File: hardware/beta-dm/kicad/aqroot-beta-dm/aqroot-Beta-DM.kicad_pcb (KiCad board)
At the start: 4 copper layers, 74 x 155 mm, 188 parts, among them J1 CH280QV10-CT_50P, J2 Molex_5025700893, J3 USB_C_Receptacle_USB2.0_16P, J4 JST-PH-2 BATTERY, J5 COMMUNITY_HEADER_2x13, J6 JST-PH-2 SPEAKER, Q1 AO3400A, SW1 BOOT, SW2 UP, SW3 DOWN, SW4 LEFT, SW5 RIGHT, SW6 A_SELECT, SW7 B_BACK, SW8 HOME, SW9 SW_SPDT, U1 ESP32-S3-WROOM-1, U10 USBLC6-2SC6, U11 BQ25185, U12 TPS63020, U13 TPS61023, U14 MAX17048, U15 TPS22918, U16 TCA9517ADGK, U17 TPS61169DCKR, U2 TCA9535PWR, U3 TCA9535PWR, U4 BMI270, U5 MAX98357A, U6 TSOP38238, U7 E07-400M10S, U8 E22-900M22S, U9 ST25R3916-AQET

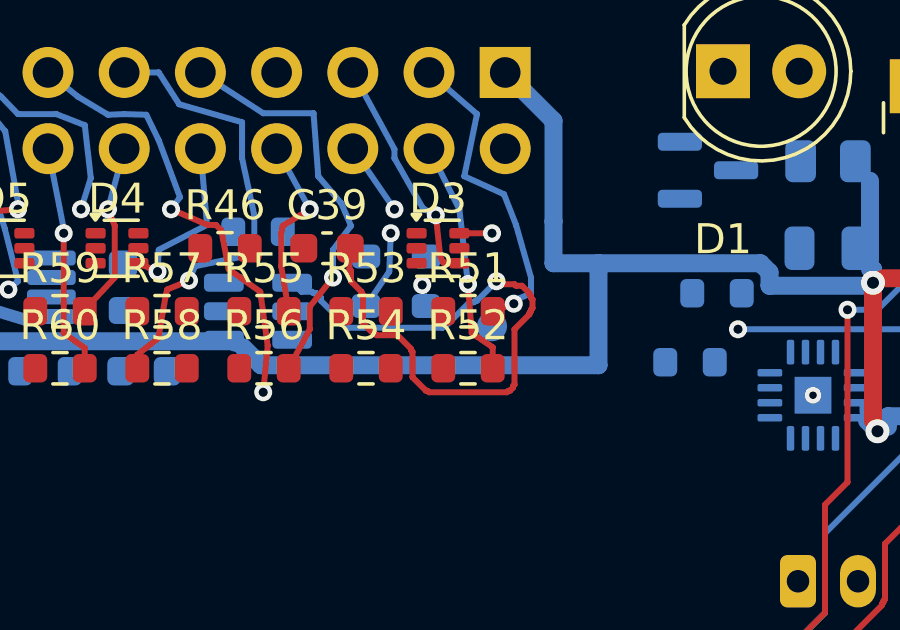
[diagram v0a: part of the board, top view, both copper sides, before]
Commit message: hardware(beta-dm): two header links routed, residual audit, BOOT_N returned
RESIDUAL NON-GND SWEEP. Every fitted must-work non-GND net was attempted under
the current locks, on regional grids, joining only islands that carry a fitted
pad so no dead DNP copper is created. 2 of 29 routed and are landed:

  /09_COMMUNITY_HEADER/XGPIO2_HDR   31 seg  2 via  15.303 mm  one island
  /09_COMMUNITY_HEADER/XGPIO3_HDR   21 seg  2 via  14.793 mm  one island

The other 27 have no path at all - not a rule, not a lock, not a keepout.
Flooding from each endpoint shows two sealed pockets of roughly 1000-3000 cells
that never touch. XGPIO6_HDR routed only partially and its 4 partial segments
were DISCARDED rather than landed; dangling copper is worse than a ratsnest
line. Completing the rest needs a dedicated header and power program that
re-plans existing copper, which is a release-set composition change and so a
STOP condition.

BOOT_N REMAINS OPEN AND IS RETURNED. Option W was ratified, replayed exactly
and validated analytically - BOOT_N 52.445 mm as one island, WAKE_INT_N
re-landed as one island with all five fitted pads, WAKE function and the J5
path through R66 intact. The KiCad scratch gate then rejected it with 11
errors, all on the replacement +3V3 escape: P3V3 requires 0.40 mm width on the
outer layers and a 0.40 mm via drill, and the previous report's claim that the
R2.1 re-join was "at ordinary rules" was wrong - the router had used the
0.20 mm default.

Re-measured at the real P3V3 rules: a 0.40 mm track escapes R2.1 only with a
0.60/0.30 via. The smallest legal P3V3 via is 0.65/0.40 (0.40 drill plus the
0.125 mm annular floor) and NO site for one exists anywhere in R2.1's pocket at
any track width; with no via at all the pocket contains no other +3V3 copper.
The largest clearance at which a compliant 0.65/0.40 via fits is 0.175 mm.

And the two demands are mutually exclusive: reserving just the 1 mm square
E6_R2_1_CLR re-seals U1.27 from 2 972 215 cells to 751. BOOT_N'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
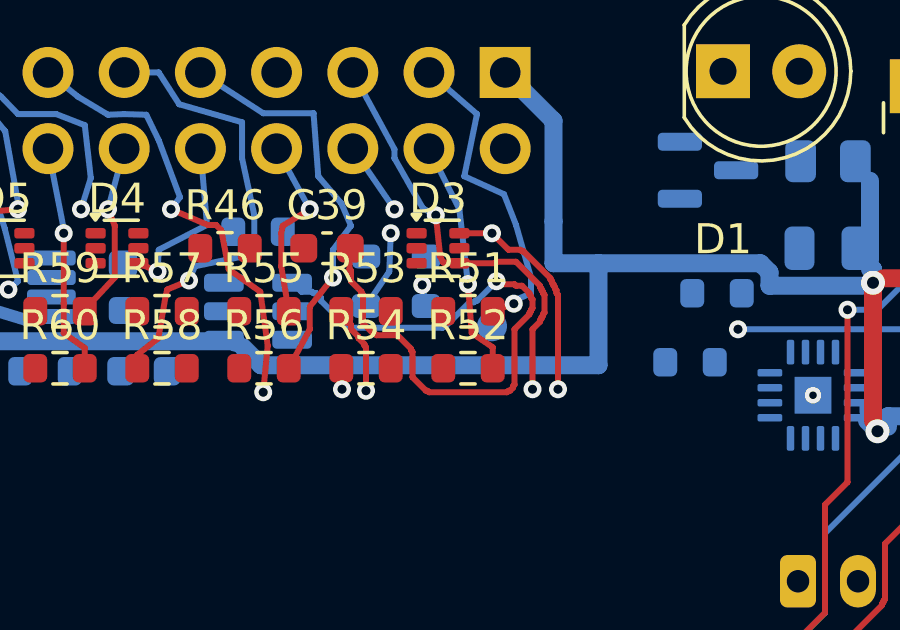
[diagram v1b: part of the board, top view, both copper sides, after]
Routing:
- net /09_COMMUNITY_HEADER/XGPIO2_HDR: track 7.77 -> 23.1 mm, vias 1 -> 3
- net /09_COMMUNITY_HEADER/XGPIO3_HDR: track 7.20 -> 22.0 mm, vias 2 -> 4

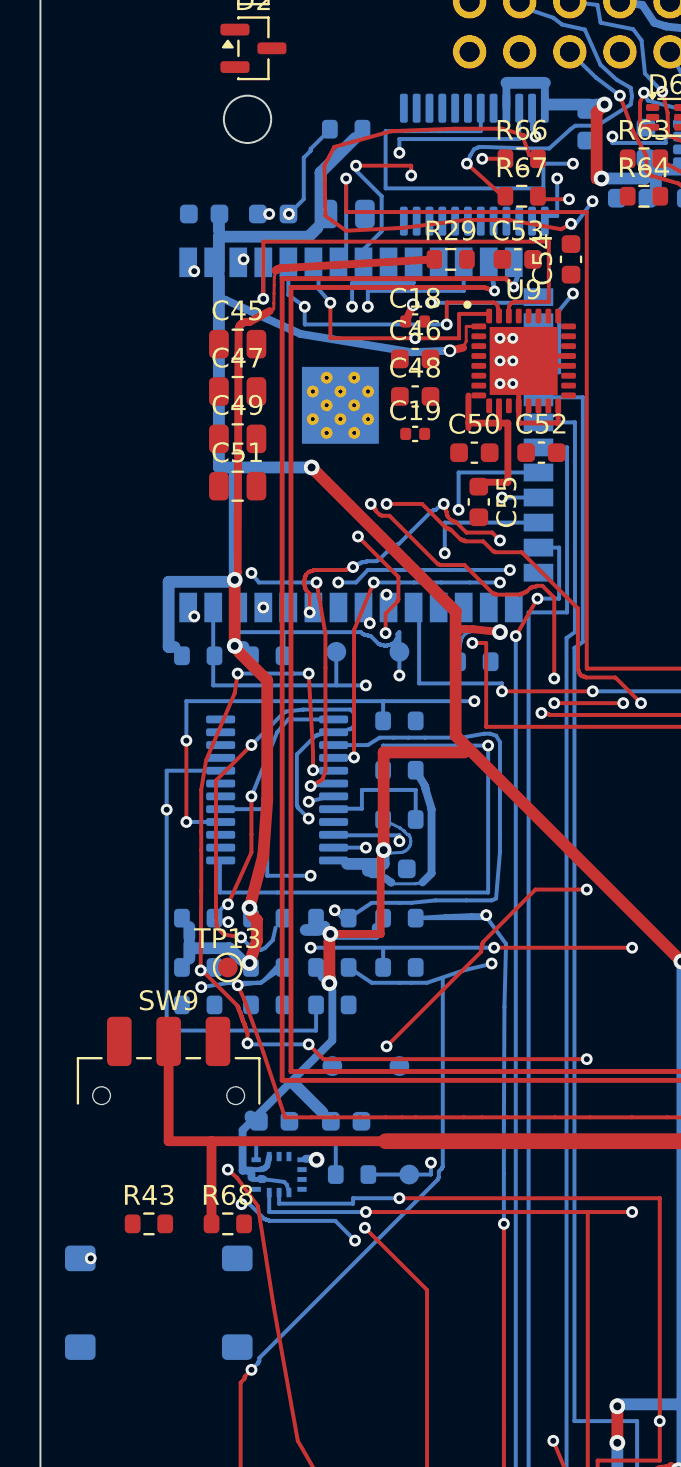
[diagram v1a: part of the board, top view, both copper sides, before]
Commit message: hardware(beta-dm): Option W landed, BOOT_N complete, no new rule exception
Implements the CTO ruling on BOOT_N. Released 38 objects - /WAKE_INT_N
(15 seg, 4 via, 68.633 mm) and the R2-local +3V3 escape (18 seg, 1 via,
5.528 mm) - then routed BOOT_N, re-landed WAKE_INT_N and re-joined R2.1.

BOOT_N       52.445 mm, 67 seg, 5 via, one island: U1.27, R2.2, both SW1.1
WAKE_INT_N   97.588 mm, 178 seg, 4 via, one island, all five fitted pads kept
             (R3.1, R66.1, U1.23, U2.1, U3.1)
+3V3 R2.1     3.531 mm, 13 seg, 1 via, rail one island

The ruling authorised a local 0.175 mm power-via clearance exception. It is
NOT needed and was NOT created. With the P3V3 outer-layer width floor
(0.40 mm) and a compliant POWER via (0.65/0.40, annular 0.125 mm) actually
applied - which the earlier attempt did not do - and with BOOT_N routed
first, the R2.1 re-join lands at the ORDINARY 0.200 mm clearance. Measured
tightest separation over all 268 new objects: 0.2000 mm against 0.200 mm.
No new rule area, no DRU change, no global change. E6_R2_1_CLR now encloses
zero P3V3 items and is inert; E6_R2_1_WIDTH encloses only 0.40 mm copper
that satisfies the unrelaxed floor.

KiCad DRC 0 errors (240 warnings, unchanged from baseline). Unconnected
223 -> 220. Preservation diff: 188 footprints, 776 pad keys, 44 zone
definitions and Edge.Cuts all identical; 0 objects modified in place.

Co-Authored-By: Claude Opus 5 <noreply@anthropic.com>
Claude-Session: https://claude.ai/code/session_01Xb8w7QRKxkkr3DtJ1wNtrp
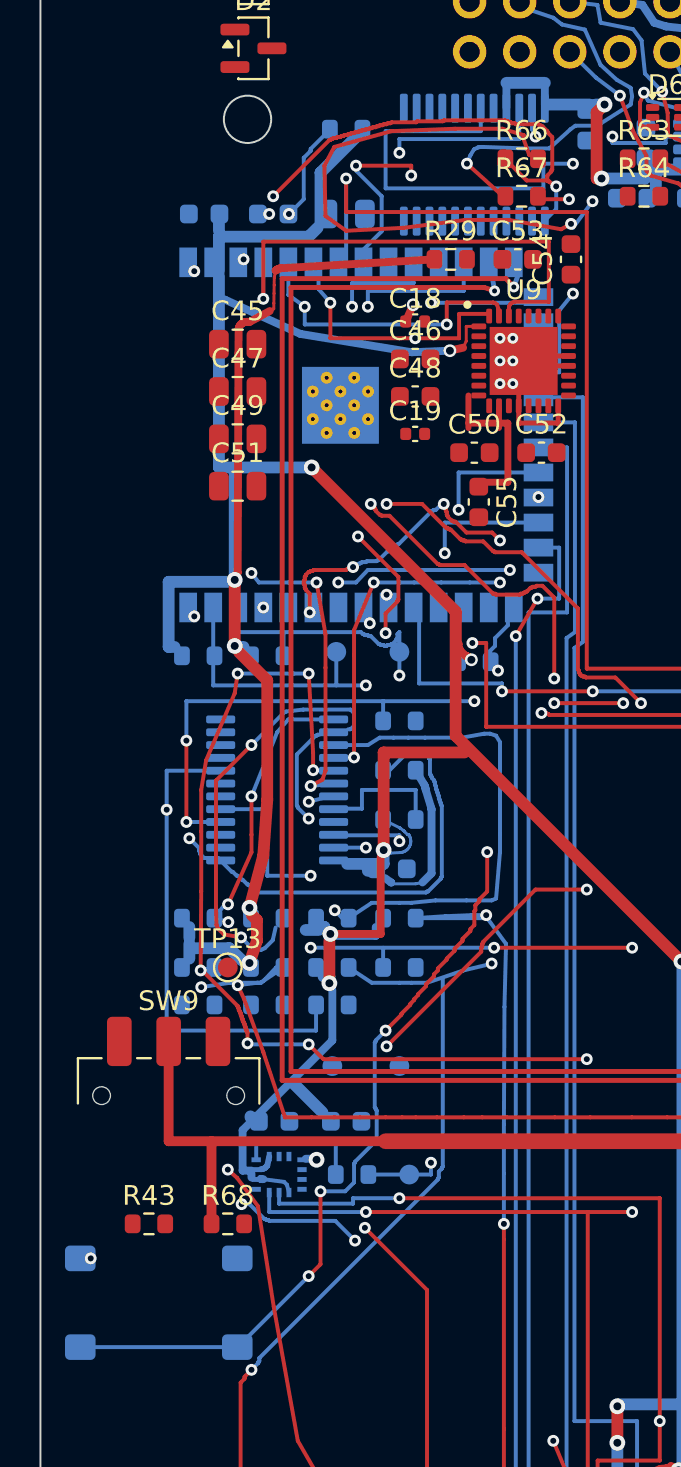
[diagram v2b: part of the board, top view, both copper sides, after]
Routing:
- net /02_MCU_CORE/BOOT_N: track 0.00 -> 52.4 mm, vias 0 -> 5
- net /WAKE_INT_N: track 68.6 -> 97.6 mm
- net +3V3: track 623.8 -> 621.8 mm

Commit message: hardware(beta-dm): active-J5 residual sweep, four must-work lines closed
With J5 kept active, every fitted J5 signal path is must-work. Re-audited the
whole fitted must-work non-GND set on the post-Option-W board and routed what
fits under the current locks:

  XGPIO6_HDR   R57.1 -> the J5.10 island   1.613 mm, 5 seg, F.Cu, one island
  Net-(SW9-A)  SW9.1 <-> U12.12 <-> R43.1  89.399 mm, 76 seg, 6 via
  ACC_3V3_SW   one join                     2.504 mm, 2 seg, B.Cu

ACC_3V3_SW resolves to the P3V3 netclass, so it is routed at the 0.40 mm
outer-layer width floor. Routing it at the 0.20 mm default produced four
track_width errors and was discarded rather than kept.

Unconnected 220 -> 216. KiCad DRC 0 errors, warnings unchanged at 240.
Preservation diff: 188 footprints, 776 pad keys, 44 zone definitions and
Edge.Cuts identical; 0 objects removed, 0 modified in place.

The remaining 31 fitted must-work joins are congestion-sealed and are NOT
routable without a new release. Evidence is in the residual doc.

Co-Authored-By: Claude Opus 5 <noreply@anthropic.com>
Claude-Session: https://claude.ai/code/session_01Xb8w7QRKxkkr3DtJ1wNtrp
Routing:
- net Net-(SW9-A): track 0.00 -> 89.4 mm, vias 0 -> 6
- net /09_COMMUNITY_HEADER/ACC_3V3_SW: track 13.3 -> 15.8 mm
- net /09_COMMUNITY_HEADER/XGPIO6_HDR: track 5.78 -> 7.40 mm

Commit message: hardware(beta-dm): R2 power via moved to (21.900, 37.400), mask dam 0.125 mm
Lands CTO candidate B. The escape via at (21.850, 37.400) was rejected on DFM:
it overlapped the R2.1 pad copper by 0.050 mm and left only a 0.075 mm
solder-mask dam to a 0.40 mm tented barrel sitting under the R2 0603 body -
below every fab minimum, with a real solder-wicking and tombstoning risk that
KiCad DRC does not test.

Minimum change: 10 of the 13 escape segments were already common to both
routes and were left untouched. Removed 3 segments + the via (a5e10000-ac94,
-7889, -ac7a, -e1e0), added 3 segments + 1 via under prefix f2b40000.

Measured on the real board after zone refill:
  via centre       21.900000, 37.400000      exact
  size / drill     0.650000 / 0.400000       annular 0.1250 mm
  P3V3 width       0.40 mm on B.Cu and F.Cu
  mask dam         0.1250 mm                 (pad_to_mask_clearance is 0, so
                                              the mask opening IS the pad copper)
  via vs R2.1      0.0000 mm  tangent, no copper overlap
  R2.2             0.2000 mm copper, 0.3250 mm drill edge - no regression
  ordinary clr     0.2000 mm tightest, no exception created
  tenting          inherited both sides, no per-via override, no paste over it

Escape 3.531 -> 3.631 mm. BOOT_N (67 seg, 5 via, 52.445 mm) and WAKE_INT_N
(178 seg, 4 via, 97.588 mm, all five fitted pads) byte-identical. BOOT_N,
WAKE_INT_N and +3V3 one island each. KiCad DRC 0 errors, 240 warnings and 216
unconnected, all unchanged. Preservation diff: 188 footprints, 776 pad keys,
44 zone definitions and Edge.Cuts identical, 0 objects modified in place.

E6_R2_1_CLR encloses 0 P3V3 items; E6_R2_1_WIDTH encloses 3, all 0.40 mm, so
candidate-B copper depends on neither. BOOT_N and WAKE_INT_N are Default class
and every E6_R2_1 rule is scoped P3V3, so inheritance is impossible. Both areas
stay in the DRU this pass - inert, retire before pours.

Beta-DM solder mask is locked to GREEN for this fabrication build 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
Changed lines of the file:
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@@
-	)
-	(segment
-		(start 21.7 37.25)
-		(end 21.65 37.25)
-		(width 0.4)
-		(layer "F.Cu")
-		(net "+3V3")
 	)
 	(segment
@@
 		(start 21.15 36.55)
 		(end 21.15 35.05)
-		(width 0.4)
-		(layer "F.Cu")
-		(net "+3V3")
-	)
-	(segment
-		(start 21.85 37.4)
-		(end 21.7 37.25)
 		(width 0.4)
 		(layer "F.Cu")
@@
 		(net "+3V3")
 	)
+	(segment
+		(start 21.75 37.25)
+		(end 21.9 37.4)
+		(width 0.4)
+		(layer "F.Cu")
+		(net "+3V3")
+	)
+	(segment
+		(start 21.65 37.25)
+		(end 21.75 37.25)
+		(width 0.4)
+		(layer "F.Cu")
+		(net "+3V3")
+	)
 	(via
 		(at 69.1 116)
@@
 		(at 69.1 86)
 		(size 0.8)
-		(drill 0.4)
-		(layers "F.Cu" "B.Cu")
-		(net "+3V3")
-	)
-	(via
-		(at 21.85 37.4)
-		(size 0.65)
 		(drill 0.4)
 		(layers "F.Cu" "B.Cu")
@@
 		(at 10.6 52.775)
 		(size 0.8)
+		(drill 0.4)
+		(layers "F.Cu" "B.Cu")
+		(net "+3V3")
+	)
+	(via
+		(at 21.9 37.4)
+		(size 0.65)
 		(drill 0.4)
 		(layers "F.Cu" "B.Cu")
@@
 	)
 	(segment
-		(start 21.3 37.4)
-		(end 21.85 37.4)
-		(width 0.4)
-		(layer "B.Cu")
-		(net "+3V3")
-	)
-	(segment
 		(start 17.4 47.05)
 		(end 17.4 47.75)
@@
 		(layer "B.Cu")
 		(net "+3V3")
+	)
+	(segment
+		(start 21.3 37.4)
+		(end 21.9 37.4)
+		(width 0.4)
+		(layer "B.Cu")
+		(net "+3V3")

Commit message: hardware(beta-dm): LAND XGPIO5 + XGPIO6 - Lean must-work non-GND reaches ZERO
Real-board landing. Ledger re-derived on the landed board:

  215 = A63 + B130 + C0 + D22      C = 0

THE AUTHORISED 0.45/0.20 VIA COULD NOT BE USED. Section 2's reasoning is
correct - /XGPIO5 is Default class and the DRU's 0.40 mm drill floor is
POWER-class only - but the binding constraint is in BOARD SETUP, not the DRU:

  rules.min_via_diameter          0.5   <- 0.45 violates this
  rules.min_through_hole_diameter 0.2   <- the 0.40/0.15 fallback violates this too

Tested rather than assumed; KiCad returned
  ERR via_diameter | min diameter 0.5000 mm; actual 0.4500 mm

Changing either would be modifying the global rules, which section 2 forbids.

LANDED INSTEAD, same result with no rule change: the web depends only on via
DIAMETER, so at the minimum legal 0.50 mm the original position still gives
only 0.0750 mm. Section 4 authorises a tiny local adjustment, and 0.050 mm of
movement suffices:

  via  (20.400, 14.100) 0.60/0.30  web 0.0250 mm
    -> (20.400, 14.050) 0.50/0.25  web 0.1250 mm   annular 0.125 mm

0.1250 mm is the PREFERRED figure, not the 0.100 mm floor. Two track endpoints
re-attached; nothing else moved.

LANDING: release 13 objects / 19.834 mm (I2C_SCL_EXT_HDR 12 + WAKE via),
added 114 segments + 9 vias.
  XGPIO5  25.775 mm, 30 seg, 3 via   ONE ISLAND
  XGPIO6 113.115 mm, 82 seg, 5 via   ONE ISLAND
  WAKE_ATTN_N_HDR {R66.2, J5.13} one path, {D7.1 DNP} isolated as before

sha256 before bdfd2cec77e40f5be560ccdc2ba0256547b36c9f21d0da4b6821c15070686a21
sha256 after  aba9c46775b503411d182e76e338f829edf06b6373ae73a29cb140d7edc9d998
uuid prefix d8c58cf6, proven absent before the write.

Preservation: footprints 0, pads 0, zones 0, Edge.Cuts 12->12. Removals touched
ONLY I2C_SCL_EXT_HDR and WAKE_ATTN_N_HDR; additions ONLY XGPIO5/6 and WAKE.
DRC after refill: 0 errors, 240 warnings, warning-type delta NONE, parity 0.
WAKE_INT_N, SX1262_RXEN, BOOT_N, +3V3 each one island and unchan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
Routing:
- net /XGPIO6: track 0.00 -> 113.1 mm, vias 0 -> 5
- net /XGPIO5: track 0.00 -> 25.8 mm, vias 0 -> 3
- net /09_COMMUNITY_HEADER/I2C_SCL_EXT_HDR: track 19.8 -> 0.00 mm, vias 2 -> 0
- net /09_COMMUNITY_HEADER/WAKE_ATTN_N_HDR: track 61.0 -> 61.6 mm
